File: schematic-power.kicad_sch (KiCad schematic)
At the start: 32 parts, among them U4 TPS62933, U9 TPS62933

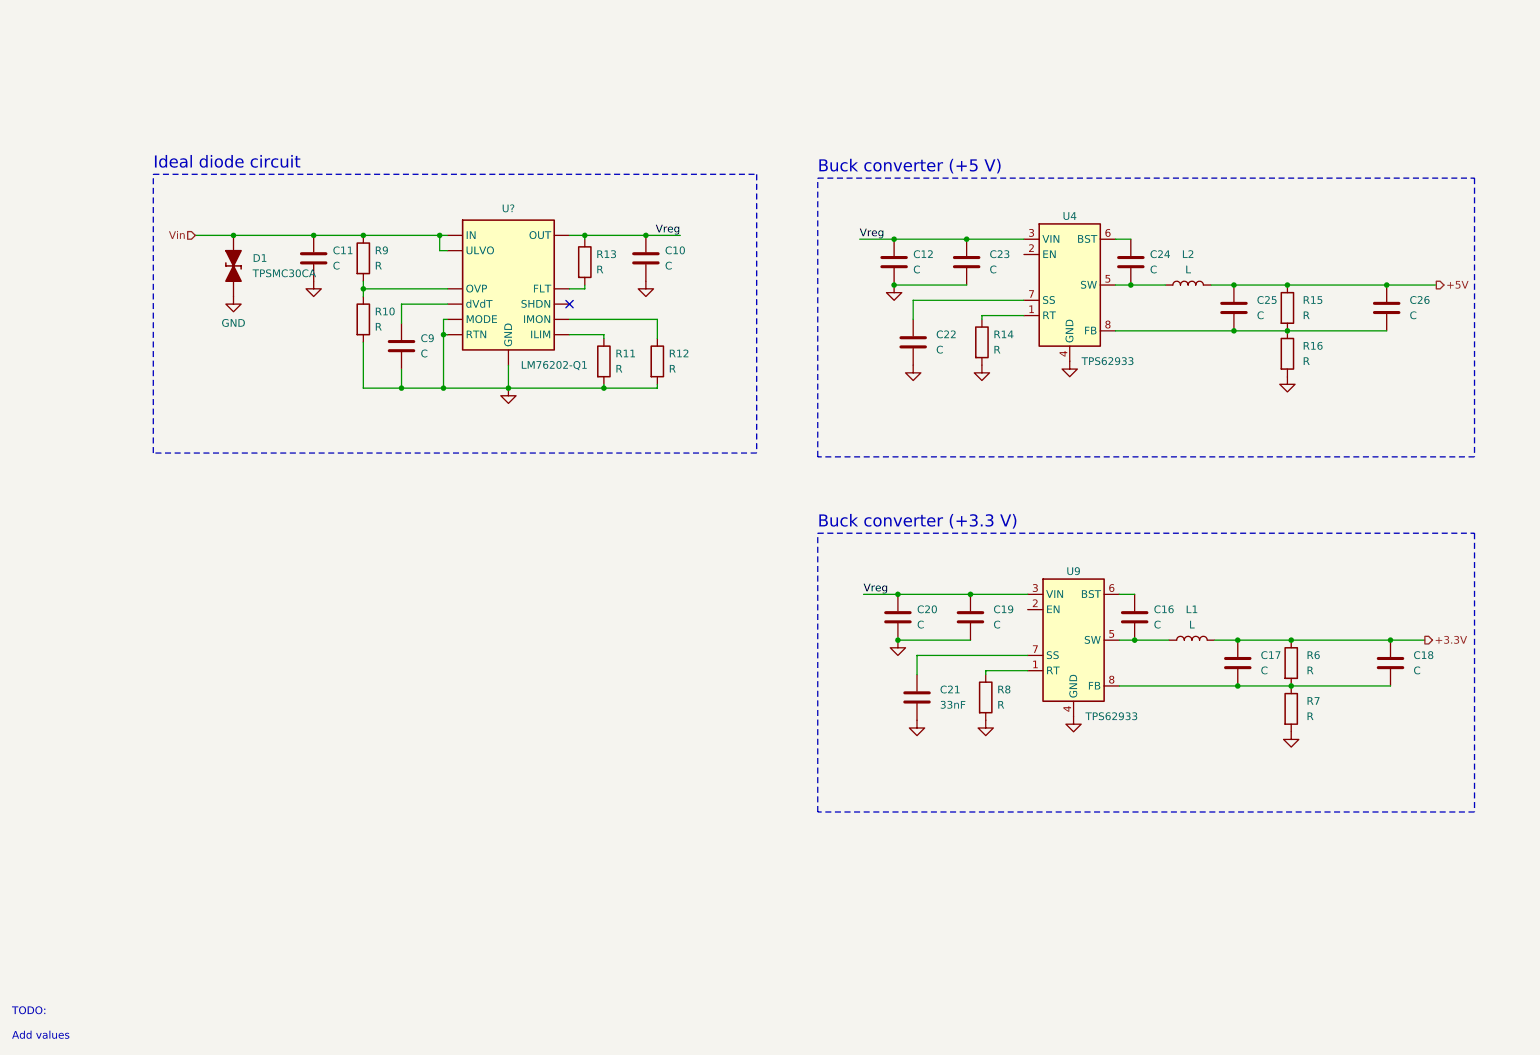
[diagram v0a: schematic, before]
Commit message: Update project structure to fit its name
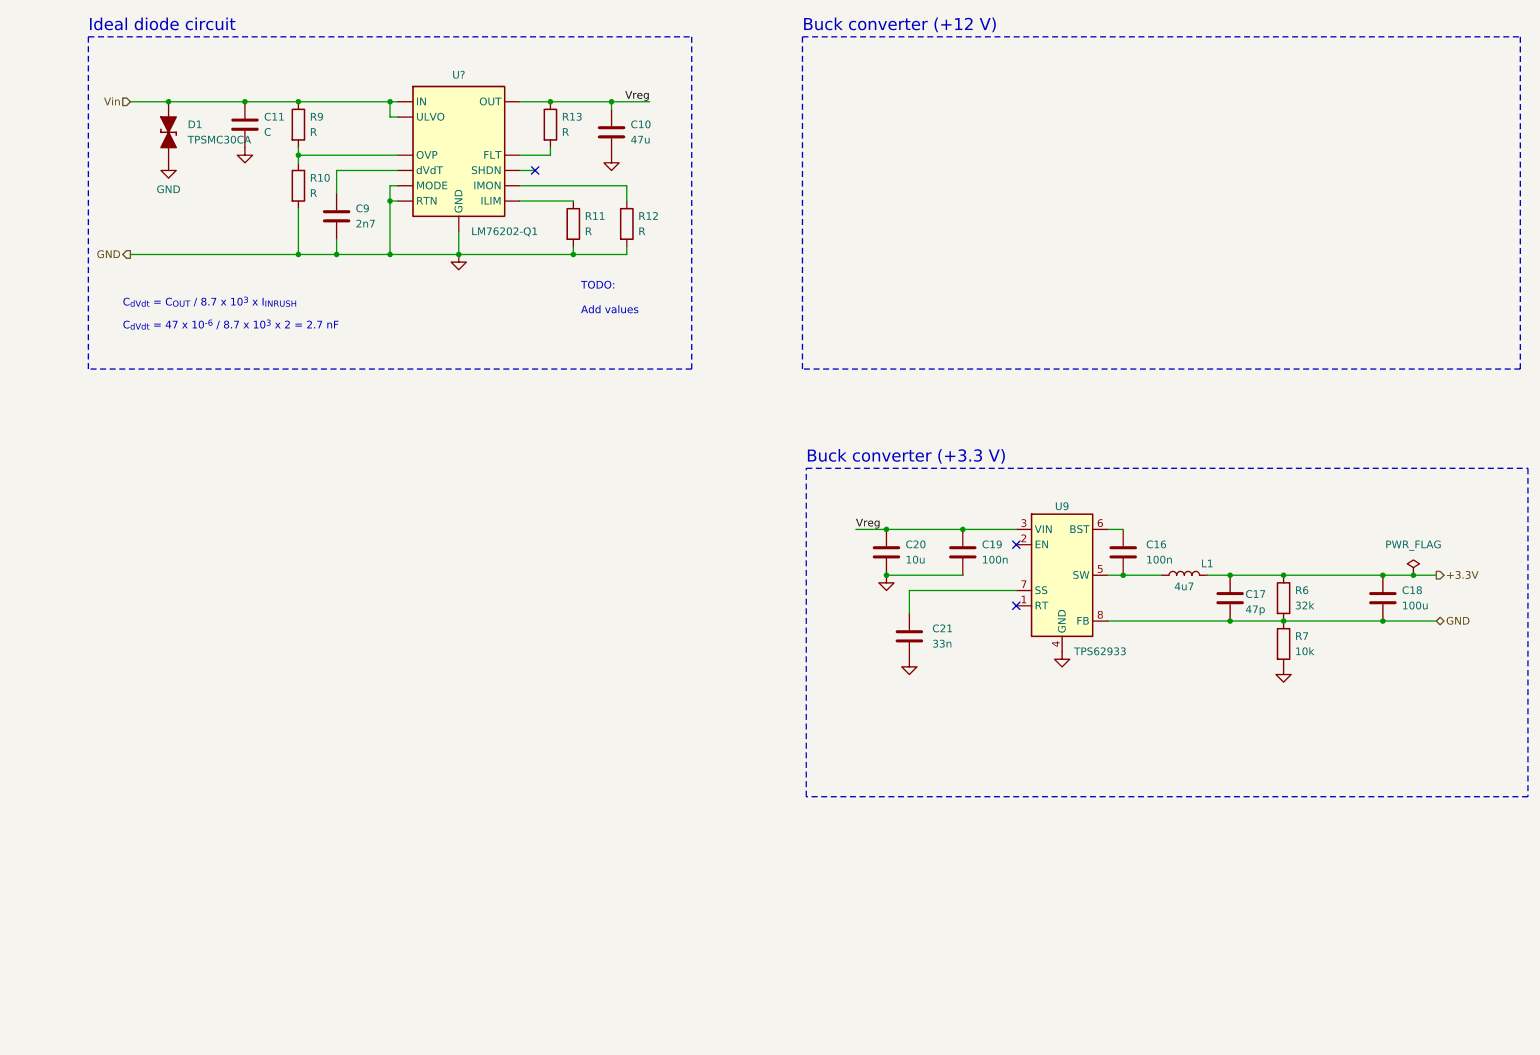
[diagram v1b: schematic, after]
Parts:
- removed C12, C22, C23, C24, C25, C26: C, symbol Device:C
- removed L2: L, symbol Device:L
- removed R14, R15, R16, R8: R, symbol Device:R
- removed U4: TPS62933, Package_TO_SOT_SMD:SOT-583-8, symbol Regulator_Switching:TPS62933
- C10: value C -> 47u
- C16, C19: value C -> 100n
- C17: value C -> 47p
- C18: value C -> 100u
- C20: value C -> 10u
- C21: value 33nF -> 33n
- C9: value C -> 2n7
- L1: value L -> 4u7
- R6: value R -> 32k
- R7: value R -> 10k
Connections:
- net GND: now also C17.2, C18.2, R6.2, R7.1, U9.8 (FB)
- no-connect marks 1 -> 3
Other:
- note added: "Buck converter (+12 V)"
- note added: "C_{dVdt} = 47 x 10^{-6} / 8.7 x 10^{3} x 2 = 2.7 nF"
- note added: "C_{dVdt} = C_{OUT} / 8.7 x 10^{3} x I_{INRUSH}"
- note removed: "Buck converter (+5 V)"
- company: (none) -> Hydrogreen Pollub
- title: (none) -> Motor driver unit
- moved on the sheet: C10, C11, C16, C17, C18, C19, C20, C21, C9, D1, L1, R10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
